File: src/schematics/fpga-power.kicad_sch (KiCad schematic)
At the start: 25 parts, among them U6 LFE5U-85F-*BG756*

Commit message: Add remaining component footprints (#79)
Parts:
- C24, C25, C26, C27, C28, C29, C30, C31, C32, C36, C37, C38, C39, C40, C41, C42, C43, C44, C45, C46, C47: footprint (none) -> Capacitor_SMD:C_0402_1005Metric
- C33, C34, C35: footprint (none) -> Capacitor_SMD:C_0603_1608Metric
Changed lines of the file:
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@@
 			)
 		)
-		(property "Footprint" ""
+		(property "Footprint" "Capacitor_SMD:C_0402_1005Metric"
 			(at 110.49 96.52 0)
 			(effects
@@
 			)
 		)
-		(property "Footprint" ""
+		(property "Footprint" "Capacitor_SMD:C_0402_1005Metric"
 			(at 146.05 96.52 0)
 			(effects
@@
 			)
 		)
-		(property "Footprint" ""
+		(property "Footprint" "Capacitor_SMD:C_0402_1005Metric"
 			(at 163.83 85.09 0)
 			(effects
@@
 			)
 		)
-		(property "Footprint" ""
+		(property "Footprint" "Capacitor_SMD:C_0603_1608Metric"
 			(at 78.74 90.17 0)
 			(effects
@@
 			)
 		)
-		(property "Footprint" ""
+		(property "Footprint" "Capacitor_SMD:C_0603_1608Metric"
 			(at 67.31 90.17 0)
 			(effects
@@
 			)
 		)
-		(property "Footprint" ""
+		(property "Footprint" "Capacitor_SMD:C_0402_1005Metric"
 			(at 238.76 90.17 0)
 			(effects
@@
 			)
 		)
-		(property "Footprint" ""
+		(property "Footprint" "Capacitor_SMD:C_0402_1005Metric"
 			(at 128.27 96.52 0)
 			(effects
@@
 			)
 		)
-		(property "Footprint" ""
+		(property "Footprint" "Capacitor_SMD:C_0402_1005Metric"
 			(at 227.33 90.17 0)
 			(effects
@@
 			)
 		)
-		(property "Footprint" ""
+		(property "Footprint" "Capacitor_SMD:C_0402_1005Metric"
 			(at 154.94 96.52 0)
 			(effects
@@
 			)
 		)
-		(property "Footprint" ""
+		(property "Footprint" "Capacitor_SMD:C_0402_1005Metric"
 			(at 101.6 85.09 0)
 			(effects
@@
 			)
 		)
-		(property "Footprint" ""
+		(property "Footprint" "Capacitor_SMD:C_0402_1005Metric"
 			(at 119.38 85.09 0)
 			(effects
@@
 			)
 		)
-		(property "Footprint" ""
+		(property "Footprint" "Capacitor_SMD:C_0402_1005Metric"
 			(at 101.6 96.52 0)
 			(effects
@@
 			)
 		)
-		(property "Footprint" ""
+		(property "Footprint" "Capacitor_SMD:C_0402_1005Metric"
 			(at 163.83 96.52 0)
 			(effects
@@
 			)
 		)
-		(property "Footprint" ""
+		(property "Footprint" "Capacitor_SMD:C_0402_1005Metric"
 			(at 137.16 85.09 0)
 			(effects
@@
 			)
 		)
-		(property "Footprint" ""
+		(property "Footprint" "Capacitor_SMD:C_0402_1005Metric"
 			(at 137.16 96.52 0)
 			(effects
@@
 			)
 		)
-		(property "Footprint" ""
+		(property "Footprint" "Capacitor_SMD:C_0402_1005Metric"
 			(at 119.38 96.52 0)
 			(effects
@@
 			)
 		)
-		(property "Footprint" ""
+		(property "Footprint" "Capacitor_SMD:C_0603_1608Metric"
 			(at 88.9 90.17 0)
 			(effects
@@
 			)
 		)
-		(property "Footprint" ""
+		(property "Footprint" "Capacitor_SMD:C_0402_1005Metric"
 			(at 172.72 85.09 0)
 			(effects
@@
 			)
 		)
-		(property "Footprint" ""
+		(property "Footprint" "Capacitor_SMD:C_0402_1005Metric"
 			(at 146.05 85.09 0)
 			(effects
@@
 			)
 		)
-		(property "Footprint" ""
+		(property "Footprint" "Capacitor_SMD:C_0402_1005Metric"
 			(at 110.49 85.09 0)
 			(effects
@@
 			)
 		)
-		(property "Footprint" ""
+		(property "Footprint" "Capacitor_SMD:C_0402_1005Metric"
 			(at 154.94 85.09 0)
 			(effects
@@
 			)
 		)
-		(property "Footprint" ""
+		(property "Footprint" "Capacitor_SMD:C_0402_1005Metric"
 			(at 172.72 96.52 0)
 			(effects
@@
 			)
 		)
-		(property "Footprint" ""
+		(property "Footprint" "Capacitor_SMD:C_0402_1005Metric"
 			(at 128.27 85.09 0)
 			(effects
@@
 			)
 		)
-		(property "Footprint" ""
+		(property "Footprint" "Capacitor_SMD:C_0402_1005Metric"
 			(at 214.63 90.17 0)
 			(effects

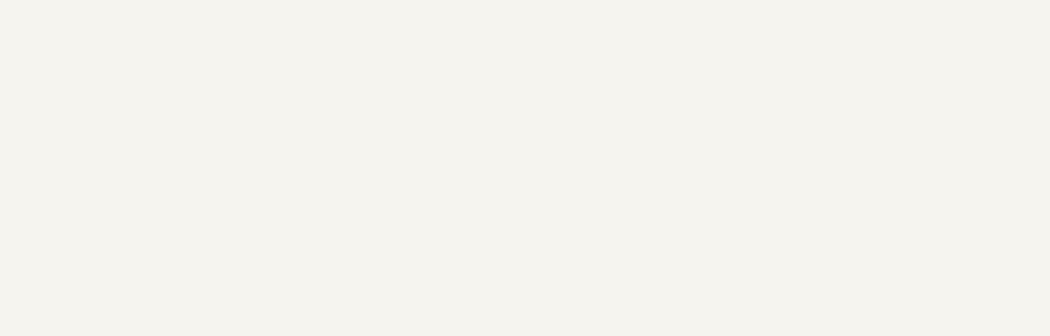
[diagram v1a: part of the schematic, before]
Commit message: Add notes on the schematic
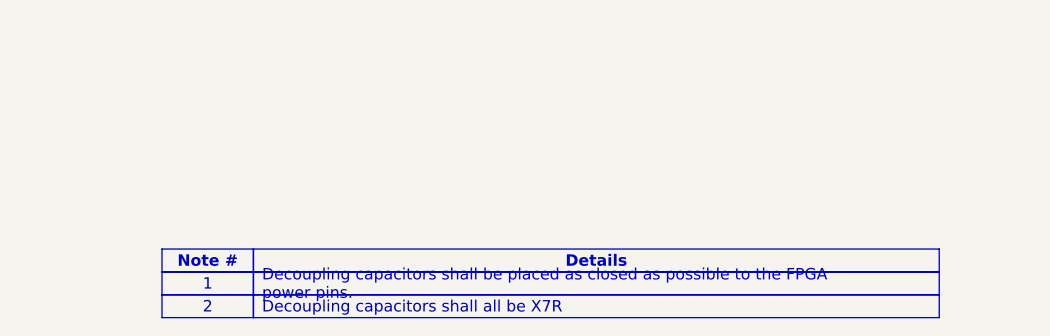
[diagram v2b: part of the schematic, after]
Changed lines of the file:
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@@
 		(comment 3 "${Part Number}")
+	)
+	(text_box "Decoupling capacitors shall all be X7R"
+		(exclude_from_sim no)
+		(at 203.2 167.64 0)
+		(size 76.2 2.54)
+		(margins 0.9525 0.9525 0.9525 0.9525)
+		(stroke
+			(width 0)
+			(type solid)
+			(color 0 0 0 1)
+		)
+		(fill
+			(type none)
+		)
+		(effects
+			(font
+				(face "Arial")
+				(size 1.27 1.27)
+				(color 0 0 0 1)
+			)
+			(justify left)
+		)
+	)
+	(text_box "Details"
+		(exclude_from_sim no)
+		(at 203.2 162.56 0)
+		(size 76.2 2.54)
+		(margins 0.9525 0.9525 0.9525 0.9525)
+		(stroke
+			(width 0)
+			(type solid)
+			(color 0 0 0 1)
+		)
+		(fill
+			(type none)
+		)
+		(effects
+			(font
+				(face "Arial")
+				(size 1.27 1.27)
+				(bold yes)
+				(color 0 0 0 1)
+			)
+		)
+	)
+	(text_box "1"
+		(exclude_from_sim no)
+		(at 193.04 165.1 0)
+		(size 10.16 2.54)
+		(margins 0.9525 0.9525 0.9525 0.9525)
+		(stroke
+			(width 0)
+			(type solid)
+			(color 0 0 0 1)
+		)
+		(fill
+			(type none)
+		)
+		(effects
+			(font
+				(face "Arial")
+				(size 1.27 1.27)
+				(color 0 0 0 1)
+			)
+		)
+	)
+	(text_box "Decoupling capacitors shall be placed as closed as possible to the FPGA power pins."
+		(exclude_from_sim no)
+		(at 203.2 165.1 0)
+		(size 76.2 2.54)
+		(margins 0.9525 0.9525 0.9525 0.9525)
+		(stroke
+			(width 0)
+			(type solid)
+			(color 0 0 0 1)
+		)
+		(fill
+			(type none)
+		)
+		(effects
+			(font
+				(face "Arial")
+				(size 1.27 1.27)
+				(color 0 0 0 1)
+			)
+			(justify left)
+		)
+	)
+	(text_box "2"
+		(exclude_from_sim no)
+		(at 193.04 167.64 0)
+		(size 10.16 2.54)
+		(margins 0.9525 0.9525 0.9525 0.9525)
+		(stroke
+			(width 0)
+			(type solid)
+			(color 0 0 0 1)
+		)
+		(fill
+			(type none)
+		)
+		(effects
+			(font
+				(face "Arial")
+				(size 1.27 1.27)
+				(color 0 0 0 1)
+			)
+		)
+	)
+	(text_box "Note #"
+		(exclude_from_sim no)
+		(at 193.04 162.56 0)
+		(size 10.16 2.54)
+		(margins 0.9525 0.9525 0.9525 0.9525)
+		(stroke
+			(width 0)
+			(type solid)
+			(color 0 0 0 1)
+		)
+		(fill
+			(type none)
+		)
+		(effects
+			(font
+				(face "Arial")
+				(size 1.27 1.27)
+				(bold yes)
+				(color 0 0 0 1)
+			)
+		)
 	)
 	(junction

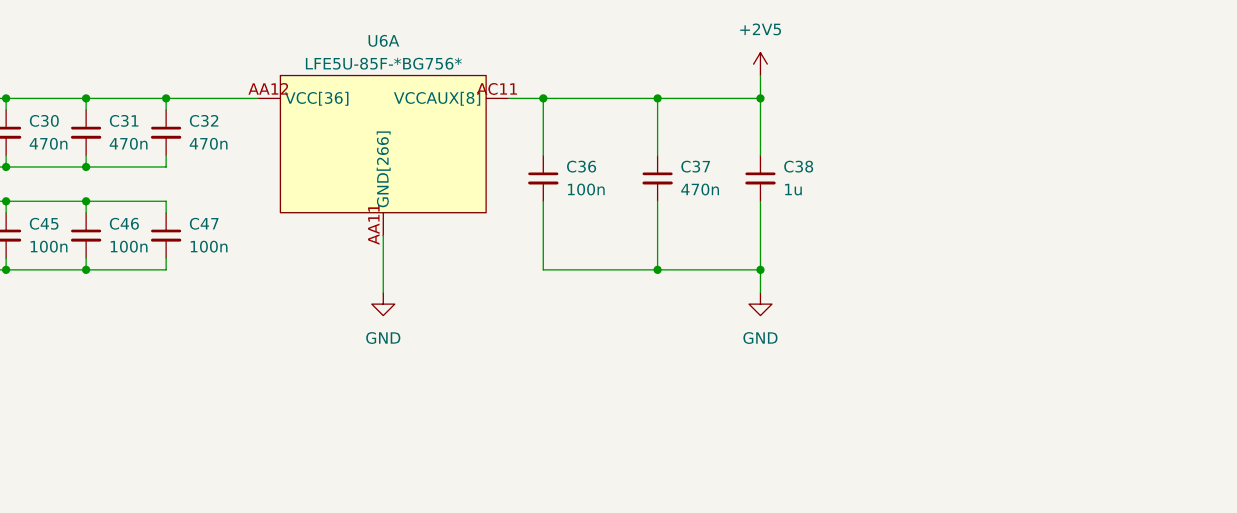
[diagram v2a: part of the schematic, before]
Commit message: Start adding power planes
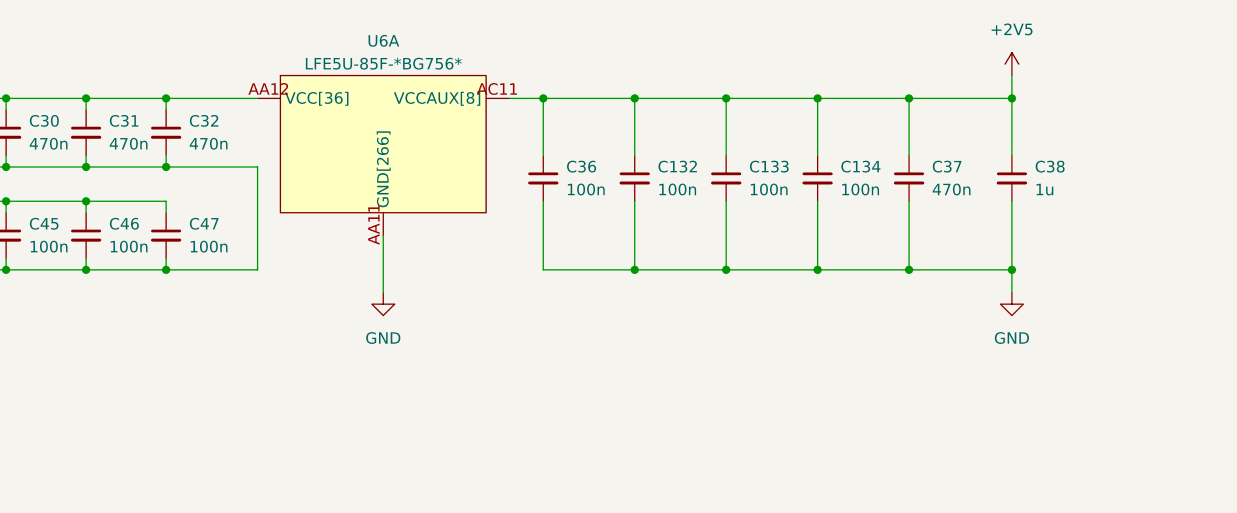
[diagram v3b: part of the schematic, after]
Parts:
- added C132, C133, C134: 100n, Capacitor_SMD:C_0402_1005Metric, symbol Device:C_Small
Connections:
- net +2V5: now also C132.1, C133.1, C134.1
- net GND: now also C24.2, C25.2, C26.2, C27.2, C28.2, C29.2, C30.2, C31.2, C32.2, C132.2, C133.2, C134.2
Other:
- moved on the sheet: C37, C38

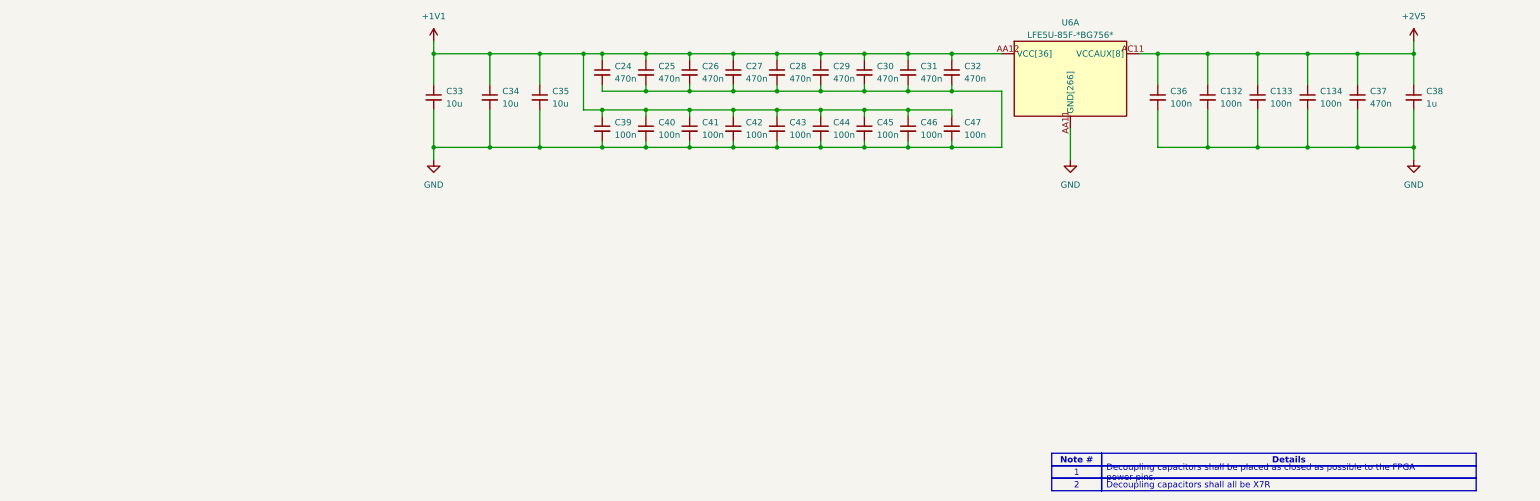
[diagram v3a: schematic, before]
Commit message: Adds decoupling capacitors
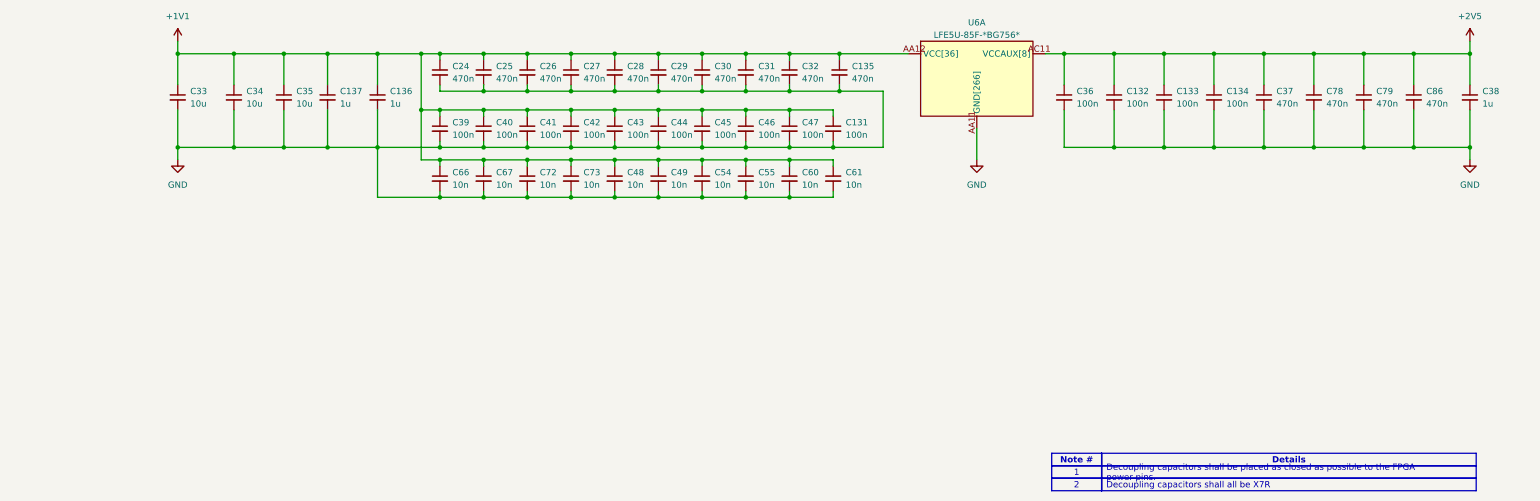
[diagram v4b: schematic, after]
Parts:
- added C131: 100n, Capacitor_SMD:C_0201_0603Metric, symbol Device:C_Small
- added C135, C78, C79, C86: 470n, Capacitor_SMD:C_0201_0603Metric, symbol Device:C_Small
- added C136, C137: 1u, Capacitor_SMD:C_0402_1005Metric, symbol Device:C_Small
- added C48, C49, C54, C55, C60, C61, C66, C67, C72, C73: 10n, Capacitor_SMD:C_0201_0603Metric, symbol Device:C_Small
- C132, C133, C134, C24, C25, C26, C27, C28, C29, C30, C31, C32, C36, C37, C39, C40, C41, C42, C43, C44, C45, C46, C47: footprint Capacitor_SMD:C_0402_1005Metric -> Capacitor_SMD:C_0201_0603Metric
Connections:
- net +1V1: now also C131.1, C135.1, C136.1, C137.1, C48.1, C49.1, C54.1, C55.1, C60.1, C61.1, C66.1, C67.1, C72.1, C73.1
- net +2V5: now also C78.1, C79.1, C86.1
- net GND: now also C131.2, C135.2, C136.2, C137.2, C48.2, C49.2, C54.2, C55.2, C60.2, C61.2, C66.2, C67.2, C72.2, C73.2, C78.2, C79.2, C86.2
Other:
- moved on the sheet: C132, C133, C134, C24, C25, C26, C27, C28, C29, C30, C31, C32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

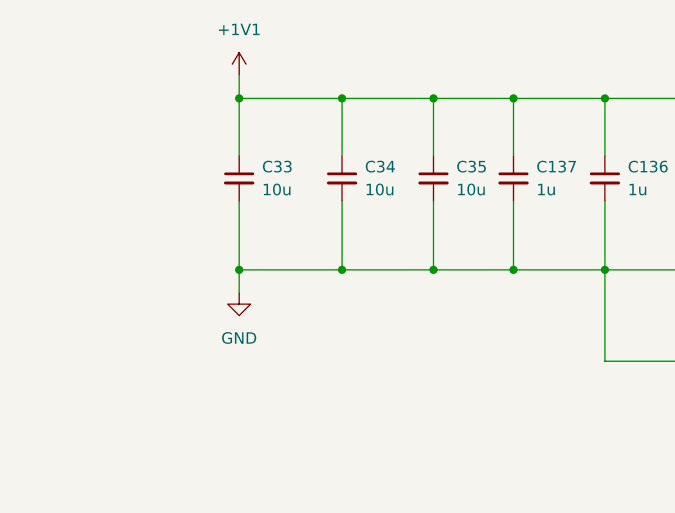
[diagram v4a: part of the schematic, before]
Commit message: Finish routing the board
* Start updating the power supply routing

* Mirror the connector pinout

* Start routing the connector

* Add second SDRAM chip

* Move decoupling capacitors to the top layer

* Add power monitoring to the schematics

* Start placing the power monitoring

* Start routing the power monitoring

* Add routing of the io connector gnd pins

* Start routing the emmc

* Fix schematic issues

* Finish routing the emmc signals, no length matching

* Fanout the ddr2

* Route the data bus of ddr2

* Route all the DDR2 signals

* Length match the ddr2 data signals

* Fix wrong interpair length matching on ddr2

* Length match the ddr2 L4 signals

* Finished routing the ddr2

* Fix missing via on ddr2 vref

* Add length matching for the emmc

* Route the internal addr bus of sdram

* Start routing the sdram data bus

* Start routing the sdrams

* Find room for sdram signals

* Finish routing the traces for the sdram

* Start assigning signals to pins for sdram

* Start routing the sram

* Cleanup memory schematic

* Apply length matching to the SDRAM

* Start routing the io connector

* fanout the io connector

* Keep routing the io connector

* Start routing the io diff pairs

* Continue routing the io connector

* Finish routing the io connector

* Route more signals in the power supply

* Finish routing all signals

* Fix ERC after routing completion

* Fix wrong annular ring constraint

* Fix DRC issues

* Cleanup tracks

* Fix diff pair skew

* Add stitching vias
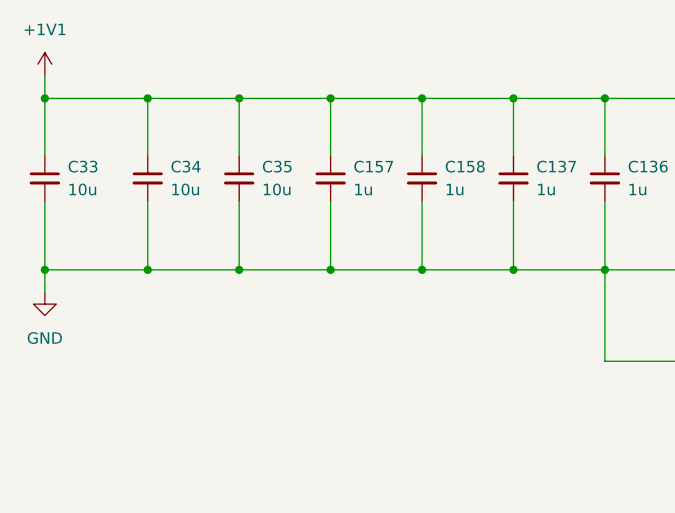
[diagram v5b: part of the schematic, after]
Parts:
- added C157, C158: 1u, Capacitor_SMD:C_0402_1005Metric, symbol Device:C_Small
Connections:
- net +1V1: now also C157.1, C158.1
- net GND: now also C157.2, C158.2
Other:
- moved on the sheet: C33, C34, C35

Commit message: Add bom components
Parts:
- C131, C132, C133, C134, C36, C39, C40, C41, C42, C43, C44, C45, C46, C47: MPN (none) -> GRM033R60J104ME19J; Manufacturer (none) -> Murata Electronics; Mouting Technology (none) -> SMD
- C135, C24, C25, C26, C27, C28, C29, C30, C31, C32, C37, C78, C79, C86: MPN (none) -> GRM033R60J474KE90J; Manufacturer (none) -> Murata Electronics; Mouting Technology (none) -> SMD
- C136, C137, C157, C158, C38: MPN (none) -> GRM155R6YA105ME11J; Manufacturer (none) -> Murata Electronics; Mouting Technology (none) -> SMD
- C33, C34, C35: MPN (none) -> C1608X7R1A106M080AT; Manufacturer (none) -> TDK; Mouting Technology (none) -> SMD
- C48, C49, C54, C55, C60, C61, C66, C67, C72, C73: MPN (none) -> GRM033R60J103KA01D; Manufacturer (none) -> Murata Electronics; Mouting Technology (none) -> SMD
- U6: MPN (none) -> LFE5U-85F-6BG756C; Manufacturer (none) -> Lattice; Mouting Technology (none) -> SMD
